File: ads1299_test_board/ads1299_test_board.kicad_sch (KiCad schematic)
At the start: 20 parts, among them U1 ADS1299

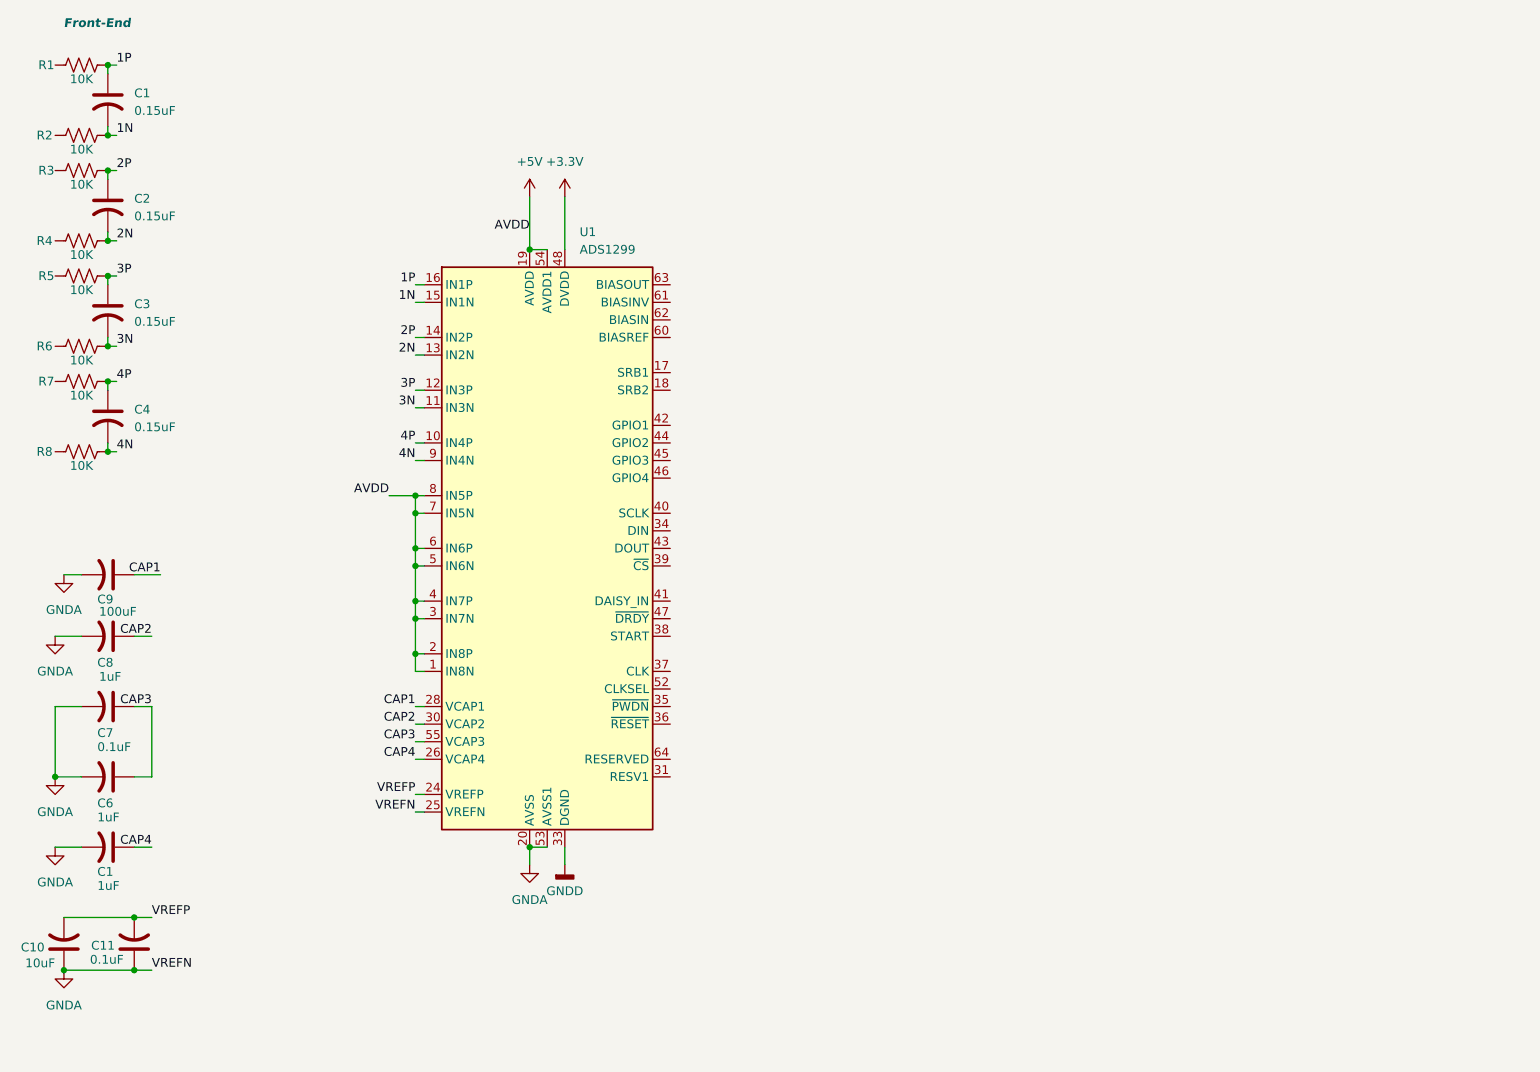
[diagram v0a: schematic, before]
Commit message: Changed the schematic architecture and made the charger schematic
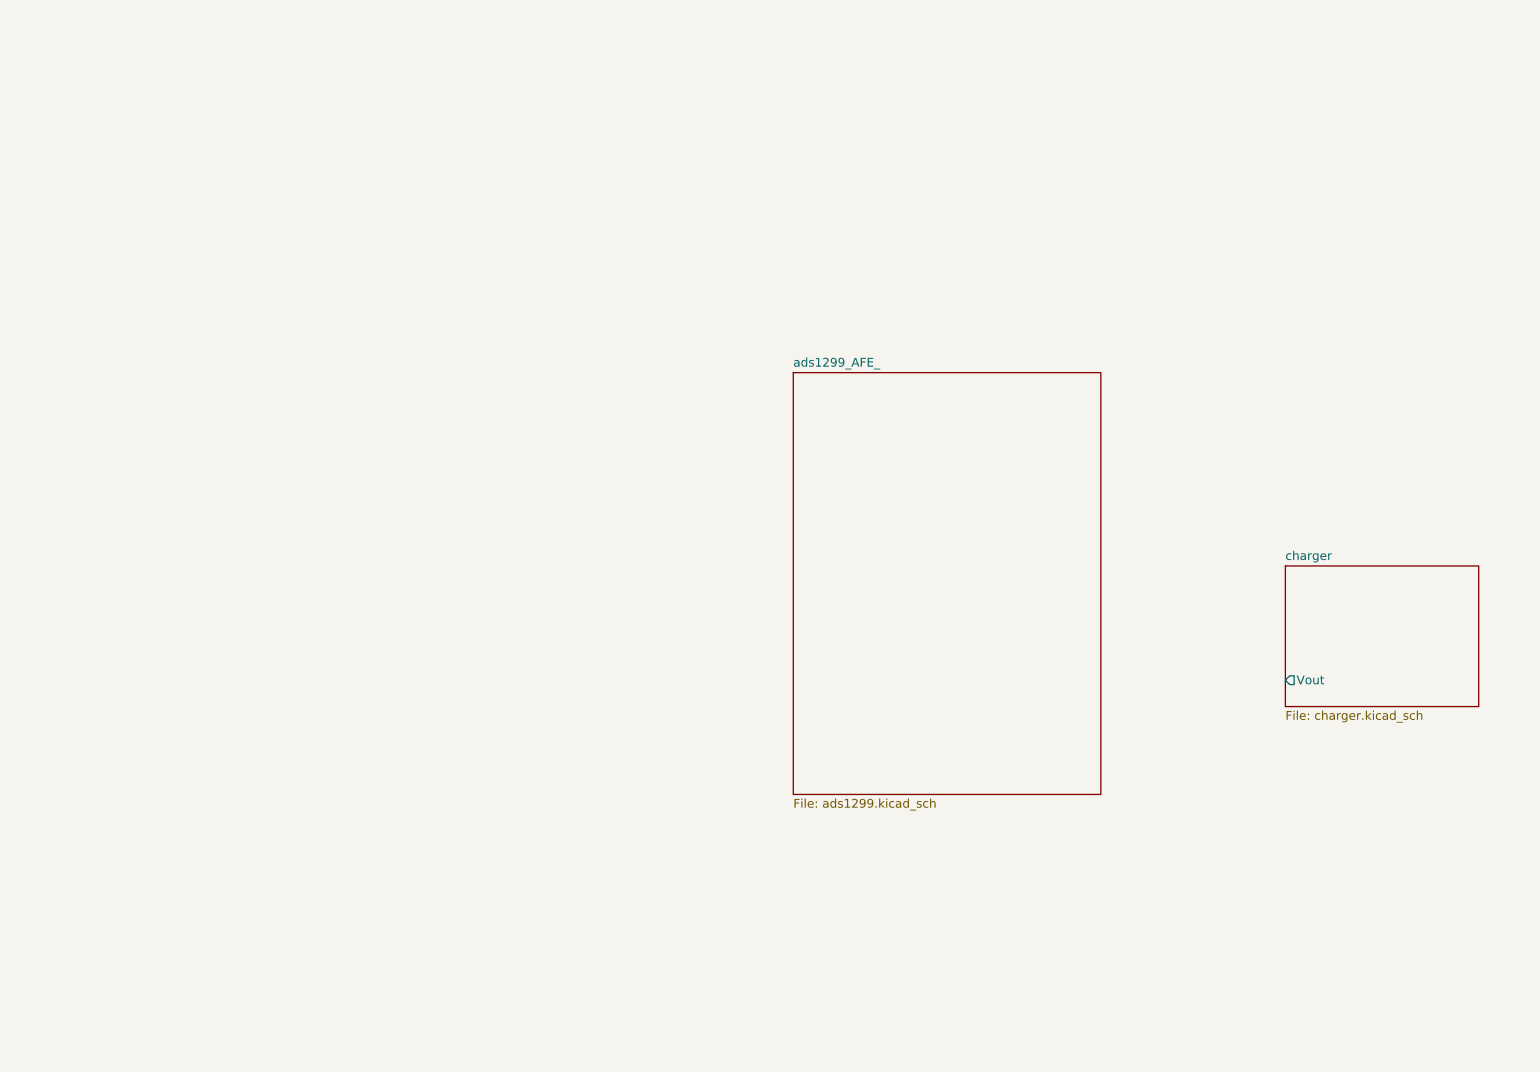
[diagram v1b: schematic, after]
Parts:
- removed C1, C6, C8: 1uF, symbol Device:C_US
- removed C1, C2, C3, C4: 0.15uF, symbol Device:C_US
- removed C10: 10uF, symbol Device:C_US
- removed C11, C7: 0.1uF, symbol Device:C_US
- removed C9: 100uF, symbol Device:C_US
- removed R1, R2, R3, R4, R5, R6, R7, R8: 10K, symbol Device:R_US
- removed U1: ADS1299, Package_QFP:TQFP-64_10x10mm_P0.5mm, symbol Analog_ADC:ADS1299
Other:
- added sheet ads1299_AFE_ (ads1299.kicad_sch)
- added sheet charger (charger.kicad_sch)
- note removed: "Front-End"

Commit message: power circuit
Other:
- added sheet power_circuit (power_circuit.kicad_sch)
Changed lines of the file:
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@@
+	)
+	(sheet
+		(at 203.2 39.37)
+		(size 27.94 48.26)
+		(exclude_from_sim no)
+		(in_bom yes)
+		(on_board yes)
+		(dnp no)
+		(fields_autoplaced yes)
+		(stroke
+			(width 0.1524)
+			(type solid)
+		)
+		(fill
+			(color 255 251 23 0.5019607843)
+		)
+		(property "Sheetname" "power_circuit"
+			(at 203.2 38.6584 0)
+			(show_name no)
+			(do_not_autoplace no)
+			(effects
+				(font
+					(size 1.27 1.27)
+				)
+				(justify left bottom)
+			)
+		)
+		(property "Sheetfile" "power_circuit.kicad_sch"
+			(at 203.2 88.2146 0)
+			(show_name no)
+			(do_not_autoplace no)
+			(effects
+				(font
+					(size 1.27 1.27)
+				)
+				(justify left top)
+			)
+		)
+		(instances
+			(project "ads1299_test_board"
+				(path "/97f9a33a-d3bd-406a-9672-b92babffe6b5"
+					(page "4")
+				)
+			)
+		)
 	)
 	(sheet

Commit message: 27/05
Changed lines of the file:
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@@
 	)
 	(sheet
-		(at 132.08 66.04)
+		(at 121.92 43.18)
 		(size 44.45 60.96)
 		(exclude_from_sim no)
@@
 		)
 		(property "Sheetname" "ads1299_AFE_"
-			(at 132.08 65.3284 0)
+			(at 121.92 42.4684 0)
 			(show_name no)
 			(do_not_autoplace no)
@@
 		)
 		(property "Sheetfile" "ads1299.kicad_sch"
-			(at 132.08 127.5846 0)
+			(at 121.92 104.7246 0)
 			(show_name no)
 			(do_not_autoplace no)

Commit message: charger circuit
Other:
- sheet ads1299_AFE_ ports: added +3.3V, +5V; removed none
- sheet charger ports: added Vbat; removed Vout
- sheet power_circuit ports: added +3.3V, +5V, Vbat; removed none
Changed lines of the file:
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@@
 	(generator_version "10.0")
 	(paper "A4")
+	(wire
+		(pts
+			(xy 181.61 44.45) (xy 203.2 44.45)
+		)
+		(stroke
+			(width 0)
+			(type default)
+		)
+	)
+	(wire
+		(pts
+			(xy 181.61 49.53) (xy 203.2 49.53)
+		)
+		(stroke
+			(width 0)
+			(type default)
+		)
+	)
+	(wire
+		(pts
+			(xy 203.2 97.79) (xy 198.12 97.79)
+		)
+		(stroke
+			(width 0)
+			(type default)
+		)
+	)
+	(wire
+		(pts
+			(xy 198.12 53.34) (xy 203.2 53.34)
+		)
+		(stroke
+			(width 0)
+			(type default)
+		)
+	)
+	(wire
+		(pts
+			(xy 198.12 97.79) (xy 198.12 53.34)
+		)
+		(stroke
+			(width 0)
+			(type default)
+		)
+	)
 	(sheet
 		(at 203.2 93.98)
@@
 			)
 		)
-		(pin "Vout" output
-			(at 203.2 110.49 180)
+		(pin "Vbat" output
+			(at 203.2 97.79 180)
 			(effects
 				(font
@@
 			)
 		)
+		(pin "+3.3V" output
+			(at 203.2 44.45 180)
+			(effects
+				(font
+					(size 1.27 1.27)
+				)
+				(justify left)
+			)
+		)
+		(pin "+5V" output
+			(at 203.2 49.53 180)
+			(effects
+				(font
+					(size 1.27 1.27)
+				)
+				(justify left)
+			)
+		)
+		(pin "Vbat" input
+			(at 203.2 53.34 180)
+			(effects
+				(font
+					(size 1.27 1.27)
+				)
+				(justify left)
+			)
+		)
 		(instances
 			(project "ads1299_test_board"
@@
 	)
 	(sheet
-		(at 121.92 43.18)
+		(at 137.16 39.37)
 		(size 44.45 60.96)
 		(exclude_from_sim no)
@@
 		)
 		(fill
-			(color 0 0 0 0)
+			(color 255 251 23 0.5019607843)
 		)
 		(property "Sheetname" "ads1299_AFE_"
-			(at 121.92 42.4684 0)
+			(at 137.16 38.6584 0)
 			(show_name no)
 			(do_not_autoplace no)
@@
 		)
 		(property "Sheetfile" "ads1299.kicad_sch"
-			(at 121.92 104.7246 0)
+			(at 137.16 100.9146 0)
 			(show_name no)
 			(do_not_autoplace no)
@@
 			)
 		)
+		(pin "+3.3V" input
+			(at 181.61 44.45 0)
+			(effects
+				(font
+					(size 1.27 1.27)
+				)
+				(justify right)
+			)
+		)
+		(pin "+5V" input
+			(at 181.61 49.53 0)
+			(effects
+				(font
+					(size 1.27 1.27)
+				)
+				(justify right)
+			)
+		)

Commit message: usb, esp32 s3 wroom 1
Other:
- added sheet ESP32_S3_WROOM (ESP32_S3_WROOM.kicad_sch)
- added sheet USB (USB.kicad_sch)
- sheet charger ports: added Vusb; removed none

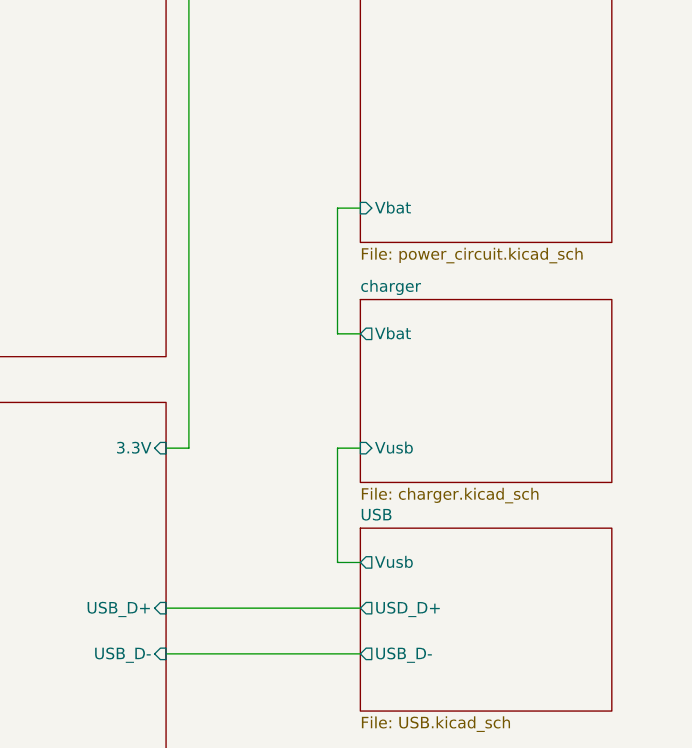
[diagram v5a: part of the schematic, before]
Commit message: usb charge and power circuit switch
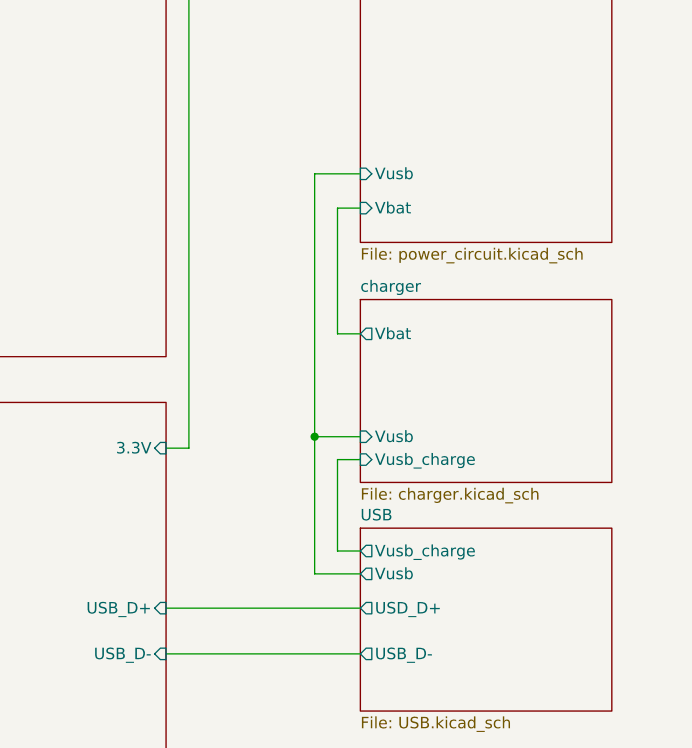
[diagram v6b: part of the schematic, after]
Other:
- sheet USB ports: added Vusb_charge; removed none
- sheet charger ports: added Vusb_charge; removed none
- sheet power_circuit ports: added Vusb; removed none
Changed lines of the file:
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@@
 	(paper "A4")
+	(junction
+		(at 163.83 107.95)
+		(diameter 0)
+		(color 0 0 0 0)
+	)
 	(junction
 		(at 149.86 46.99)
@@
 	(wire
 		(pts
+			(xy 168.91 78.74) (xy 163.83 78.74)
+		)
+		(stroke
+			(width 0)
+			(type default)
+		)
+	)
+	(wire
+		(pts
 			(xy 147.32 127) (xy 168.91 127)
 		)
@@
 	(wire
 		(pts
-			(xy 168.91 121.92) (xy 166.37 121.92)
+			(xy 168.91 123.19) (xy 163.83 123.19)
 		)
 		(stroke
@@
 	(wire
 		(pts
-			(xy 166.37 121.92) (xy 166.37 109.22)
+			(xy 163.83 123.19) (xy 163.83 107.95)
+		)
+		(stroke
+			(width 0)
+			(type default)
+		)
+	)
+	(wire
+		(pts
+			(xy 168.91 120.65) (xy 166.37 120.65)
+		)
+		(stroke
+			(width 0)
+			(type default)
+		)
+	)
+	(wire
+		(pts
+			(xy 166.37 110.49) (xy 168.91 110.49)
+		)
+		(stroke
+			(width 0)
+			(type default)
+		)
+	)
+	(wire
+		(pts
+			(xy 166.37 120.65) (xy 166.37 110.49)
 		)
 		(stroke
@@
 	(wire
 		(pts
-			(xy 166.37 109.22) (xy 168.91 109.22)
+			(xy 163.83 107.95) (xy 168.91 107.95)
 		)
 		(stroke
@@
 		(pts
 			(xy 149.86 46.99) (xy 149.86 109.22)
+		)
+		(stroke
+			(width 0)
+			(type default)
+		)
+	)
+	(wire
+		(pts
+			(xy 163.83 78.74) (xy 163.83 107.95)
 		)
 		(stroke
@@
 		)
 		(pin "Vusb" input
-			(at 168.91 109.22 180)
+			(at 168.91 107.95 180)
+			(effects
+				(font
+					(size 1.27 1.27)
+				)
+				(justify left)
+			)
+		)
+		(pin "Vusb_charge" input
+			(at 168.91 110.49 180)
 			(effects
 				(font
@@
 		)
 		(pin "Vusb" output
-			(at 168.91 121.92 180)
+			(at 168.91 123.19 180)
+			(effects
+				(font
+					(size 1.27 1.27)
+				)
+				(justify left)
+			)
+		)
+		(pin "Vusb_charge" output
+			(at 168.91 120.65 180)
 			(effects
 				(font
@@
 			(effects
 				(font
+					(size 1.27 1.27)
+				)
+				(justify left)
+			)
+		)
+		(pin "Vusb" input
+			(at 168.91 78.74 180)
+			(effects
+				(font

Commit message: work on ads1299 schematic
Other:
- sheet ads1299_AFE_ ports: added CS, DIN, DOUT, DRDY, Power_ads1299, Reset_ads1299, SCLK, Start; removed none
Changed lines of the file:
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@@
 	(paper "A4")
 	(junction
-		(at 163.83 107.95)
+		(at 177.8 107.95)
 		(diameter 0)
 		(color 0 0 0 0)
@@
 	(wire
 		(pts
-			(xy 168.91 96.52) (xy 166.37 96.52)
+			(xy 182.88 96.52) (xy 180.34 96.52)
 		)
 		(stroke
@@
 	(wire
 		(pts
-			(xy 168.91 78.74) (xy 163.83 78.74)
-		)
-		(stroke
-			(width 0)
-			(type default)
-		)
-	)
-	(wire
-		(pts
-			(xy 147.32 127) (xy 168.91 127)
-		)
-		(stroke
-			(width 0)
-			(type default)
-		)
-	)
-	(wire
-		(pts
-			(xy 166.37 82.55) (xy 168.91 82.55)
-		)
-		(stroke
-			(width 0)
-			(type default)
-		)
-	)
-	(wire
-		(pts
-			(xy 168.91 123.19) (xy 163.83 123.19)
-		)
-		(stroke
-			(width 0)
-			(type default)
-		)
-	)
-	(wire
-		(pts
-			(xy 147.32 132.08) (xy 168.91 132.08)
-		)
-		(stroke
-			(width 0)
-			(type default)
-		)
-	)
-	(wire
-		(pts
-			(xy 163.83 123.19) (xy 163.83 107.95)
-		)
-		(stroke
-			(width 0)
-			(type default)
-		)
-	)
-	(wire
-		(pts
-			(xy 168.91 120.65) (xy 166.37 120.65)
-		)
-		(stroke
-			(width 0)
-			(type default)
-		)
-	)
-	(wire
-		(pts
-			(xy 166.37 110.49) (xy 168.91 110.49)
-		)
-		(stroke
-			(width 0)
-			(type default)
-		)
-	)
-	(wire
-		(pts
-			(xy 166.37 120.65) (xy 166.37 110.49)
+			(xy 182.88 78.74) (xy 177.8 78.74)
+		)
+		(stroke
+			(width 0)
+			(type default)
+		)
+	)
+	(wire
+		(pts
+			(xy 147.32 127) (xy 182.88 127)
+		)
+		(stroke
+			(width 0)
+			(type default)
+		)
+	)
+	(wire
+		(pts
+			(xy 180.34 82.55) (xy 182.88 82.55)
+		)
+		(stroke
+			(width 0)
+			(type default)
+		)
+	)
+	(wire
+		(pts
+			(xy 182.88 123.19) (xy 177.8 123.19)
+		)
+		(stroke
+			(width 0)
+			(type default)
+		)
+	)
+	(wire
+		(pts
+			(xy 147.32 132.08) (xy 182.88 132.08)
+		)
+		(stroke
+			(width 0)
+			(type default)
+		)
+	)
+	(wire
+		(pts
+			(xy 177.8 123.19) (xy 177.8 107.95)
+		)
+		(stroke
+			(width 0)
+			(type default)
+		)
+	)
+	(wire
+		(pts
+			(xy 182.88 120.65) (xy 180.34 120.65)
+		)
+		(stroke
+			(width 0)
+			(type default)
+		)
+	)
+	(wire
+		(pts
+			(xy 180.34 110.49) (xy 182.88 110.49)
+		)
+		(stroke
+			(width 0)
+			(type default)
+		)
+	)
+	(wire
+		(pts
+			(xy 180.34 120.65) (xy 180.34 110.49)
 		)
 		(stroke
@@
 	(wire
 		(pts
-			(xy 147.32 41.91) (xy 168.91 41.91)
-		)
-		(stroke
-			(width 0)
-			(type default)
-		)
-	)
-	(wire
-		(pts
-			(xy 163.83 107.95) (xy 168.91 107.95)
-		)
-		(stroke
-			(width 0)
-			(type default)
-		)
-	)
-	(wire
-		(pts
-			(xy 149.86 46.99) (xy 168.91 46.99)
-		)
-		(stroke
-			(width 0)
-			(type default)
-		)
-	)
-	(wire
-		(pts
-			(xy 166.37 96.52) (xy 166.37 82.55)
+			(xy 147.32 41.91) (xy 182.88 41.91)
+		)
+		(stroke
+			(width 0)
+			(type default)
+		)
+	)
+	(wire
+		(pts
+			(xy 177.8 107.95) (xy 182.88 107.95)
+		)
+		(stroke
+			(width 0)
+			(type default)
+		)
+	)
+	(wire
+		(pts
+			(xy 149.86 46.99) (xy 182.88 46.99)
+		)
+		(stroke
+			(width 0)
+			(type default)
+		)
+	)
+	(wire
+		(pts
+			(xy 180.34 96.52) (xy 180.34 82.55)
 		)
 		(stroke
@@
 	(wire
 		(pts
-			(xy 163.83 78.74) (xy 163.83 107.95)
+			(xy 177.8 78.74) (xy 177.8 107.95)
 		)
 		(stroke
@@
 	)
 	(sheet
-		(at 168.91 92.71)
+		(at 182.88 92.71)
 		(size 27.94 20.32)
 		(exclude_from_sim no)
@@
 		)
 		(property "Sheetname" "charger"
-			(at 168.91 91.9984 0)
+			(at 182.88 91.9984 0)
 			(show_name no)
 			(do_not_autoplace no)
@@
 		)
 		(property "Sheetfile" "charger.kicad_sch"
-			(at 168.91 113.6146 0)
+			(at 182.88 113.6146 0)
 			(show_name no)
 			(do_not_autoplace no)
@@
 		)
 		(pin "Vbat" output
-			(at 168.91 96.52 180)
+			(at 182.88 96.52 180)
 			(effects
 				(font
@@
 		)
 		(pin "Vusb" input
-			(at 168.91 107.95 180)
+			(at 182.88 107.95 180)
 			(effects
 				(font
@@
 		)
 		(pin "Vusb_charge" input
-			(at 168.91 110.49 180)
+			(at 182.88 110.49 180)
 			(effects
 				(font
@@
 	)
 	(sheet
-		(at 168.91 118.11)
+		(at 182.88 118.11)
 		(size 27.94 20.32)
 		(exclude_from_sim no)
@@
 		)
 		(property "Sheetname" "USB"
-			(at 168.91 117.3984 0)
+			(at 182.88 117.3984 0)
 			(show_name no)
 			(do_not_autoplace no)
@@
 		)
 		(property "Sheetfile" "USB.kicad_sch"
-			(at 168.91 139.0146 0)
+			(at 182.88 139.0146 0)
 			(show_name no)
 			(do_not_autoplace no)
@@
 		)
 		(pin "USB_D-" output
-			(at 168.91 132.08 180)
+			(at 182.88 132.08 180)
 			(effects
 				(font
@@
 		)
 		(pin "USD_D+" output
-			(at 168.91 127 180)
+			(at 182.88 127 180)
 			(effects
 				(font
@@
 		)
 		(pin "Vusb" output
-			(at 168.91 123.19 180)
+			(at 182.88 123.19 180)
 			(effects
 				(font
@@
 		)
 		(pin "Vusb_charge" output
-			(at 168.91 120.65 180)
+			(at 182.88 120.65 180)
 			(effects
 				(font
@@
 	)
 	(sheet
-		(at 168.91 38.1)
+		(at 182.88 38.1)
 		(size 27.94 48.26)
 		(exclude_from_sim no)
@@
 		)
 		(property "Sheetname" "power_circuit"
-			(at 168.91 37.3884 0)
+			(at 182.88 37.3884 0)
 			(show_name no)
 			(do_not_autoplace no)
@@
 		)
 		(property "Sheetfile" "power_circuit.kicad_sch"
-			(at 168.91 86.9446 0)
+			(at 182.88 86.9446 0)
 			(show_name no)
 			(do_not_autoplace no)
@@
 		)
 		(pin "+3.3V" output
-			(at 168.91 46.99 180)
+			(at 182.88 46.99 180)
 			(effects
 				(font
@@
 		)
 		(pin "+5V" output
-			(at 168.91 41.91 180)
+			(at 182.88 41.91 180)
 			(effects
 				(font
@@
 		)
 		(pin "Vbat" input
-			(at 168.91 82.55 180)
+			(at 182.88 82.55 180)
 			(effects
 				(font
@@
 		)
 		(pin "Vusb" input
-			(at 168.91 78.74 180)
+			(at 182.88 78.74 180)
 			(effects
 				(font
@@
 			(effects
 				(font
+					(size 1.27 1.27)
+				)
+				(justify right)
+			)
+		)
+		(pin "DRDY" output
+			(at 147.32 71.12 0)
+			(effects
+				(font
+					(size 1.27 1.27)
+				)
+				(justify right)
+			)
+		)
+		(pin "Reset_ads1299" input
+			(at 147.32 91.44 0)
+			(effects
+				(font
+					(size 1.27 1.27)
+				)
+				(justify right)
+			)
+		)
+		(pin "CS" input
+			(at 147.32 82.55 0)
+			(effects
+				(font
+					(size 1.27 1.27)
+				)
+				(justify right)
+			)
+		)
+		(pin "DIN" input
+			(at 147.32 77.47 0)
+			(effects
+				(font
+					(size 1.27 1.27)
+				)
+				(justify right)
+			)
+		)
+		(pin "DOUT" output
+			(at 147.32 80.01 0)
+			(effects
+				(font
+					(size 1.27 1.27)
+				)
+				(justify right)
+			)
+		)
+		(pin "Power_ads1299" input
+			(at 147.32 93.98 0)
+			(effects
+				(font
+					(size 1.27 1.27)
+				)
+				(justify right)
+			)
+		)
+		(pin "SCLK" output
+			(at 147.32 74.93 0)
+			(effects
+				(font
+					(size 1.27 1.27)
+				)
+				(justify right)
+			)
+		)
+		(pin "Start" input
+			(at 147.32 67.31 0)
+			(effects
+				(font

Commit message: GPIO, SRB
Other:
- sheet ESP32_S3_WROOM ports: added CS, DIN, DOUT, DRDY, GPIO1, GPIO2, GPIO3, GPIO4, Power_ads1299, Reset_ads1299, SCLK, Start; removed none
- sheet ads1299_AFE_ ports: added GPIO1, GPIO2, GPIO3, GPIO4; removed none
